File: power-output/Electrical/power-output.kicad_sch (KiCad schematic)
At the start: 27 parts, among them J1 Conn_01x02_Socket, P1 USB_C_Plug_USB2.0, U1 AP2112K-3.3, U2 FUSB302BMPX, U3 LM78L05_SO8, U4 ESP8266EX, U5 CP2102N-Axx-xQFN28

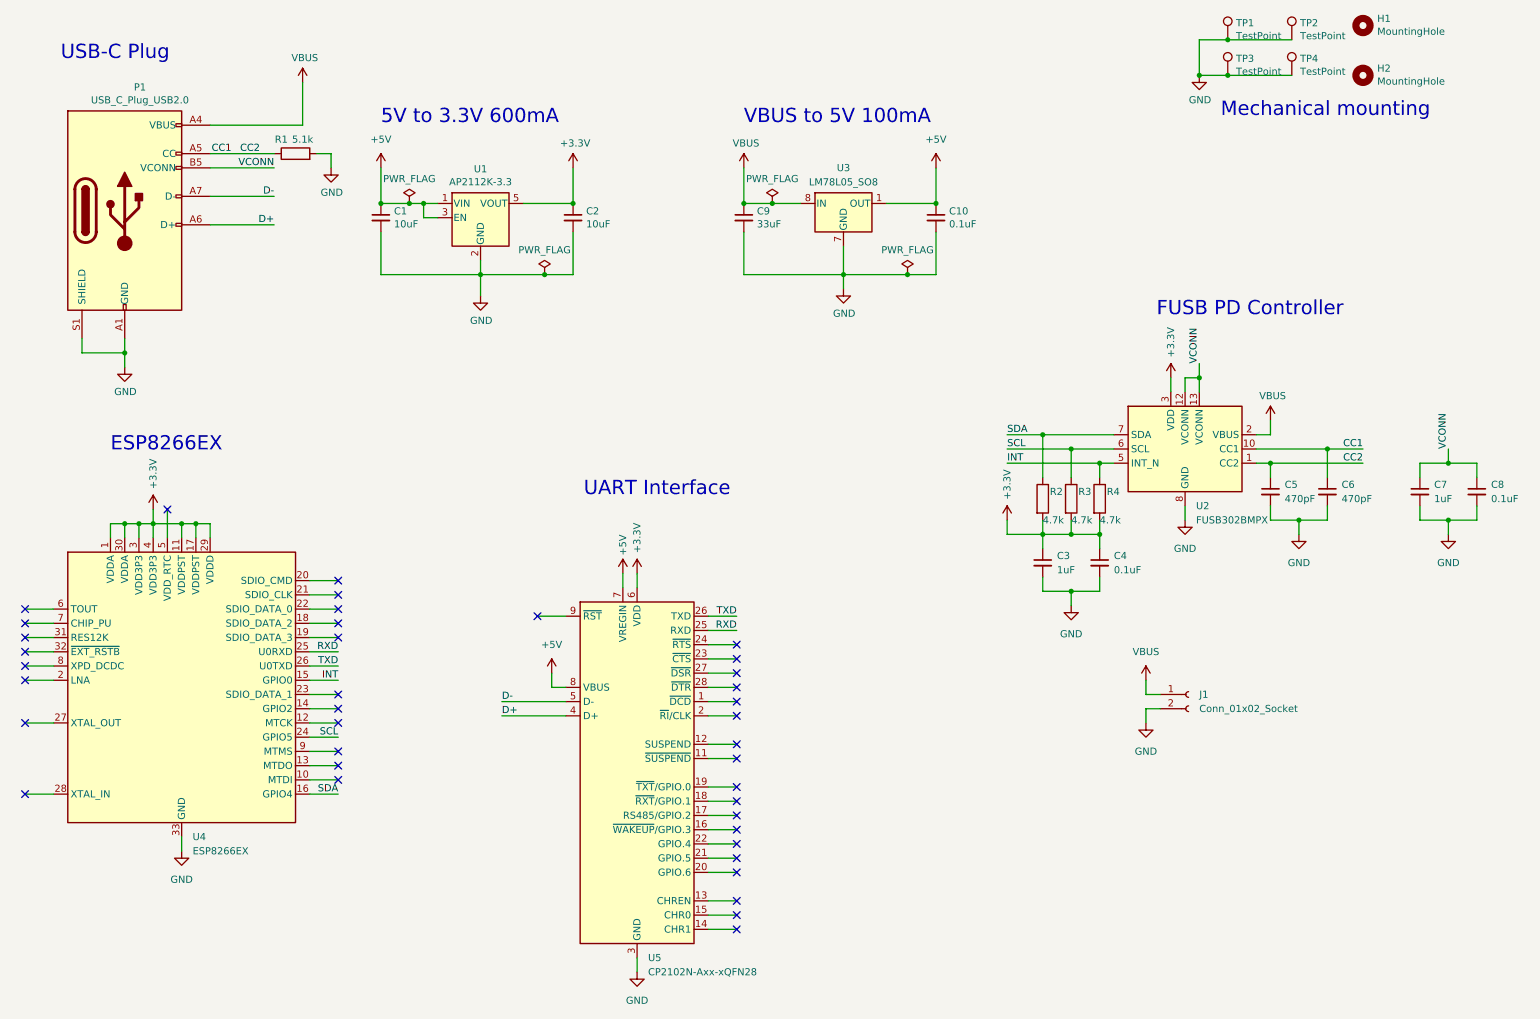
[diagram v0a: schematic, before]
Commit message: Cleaned Up power-output
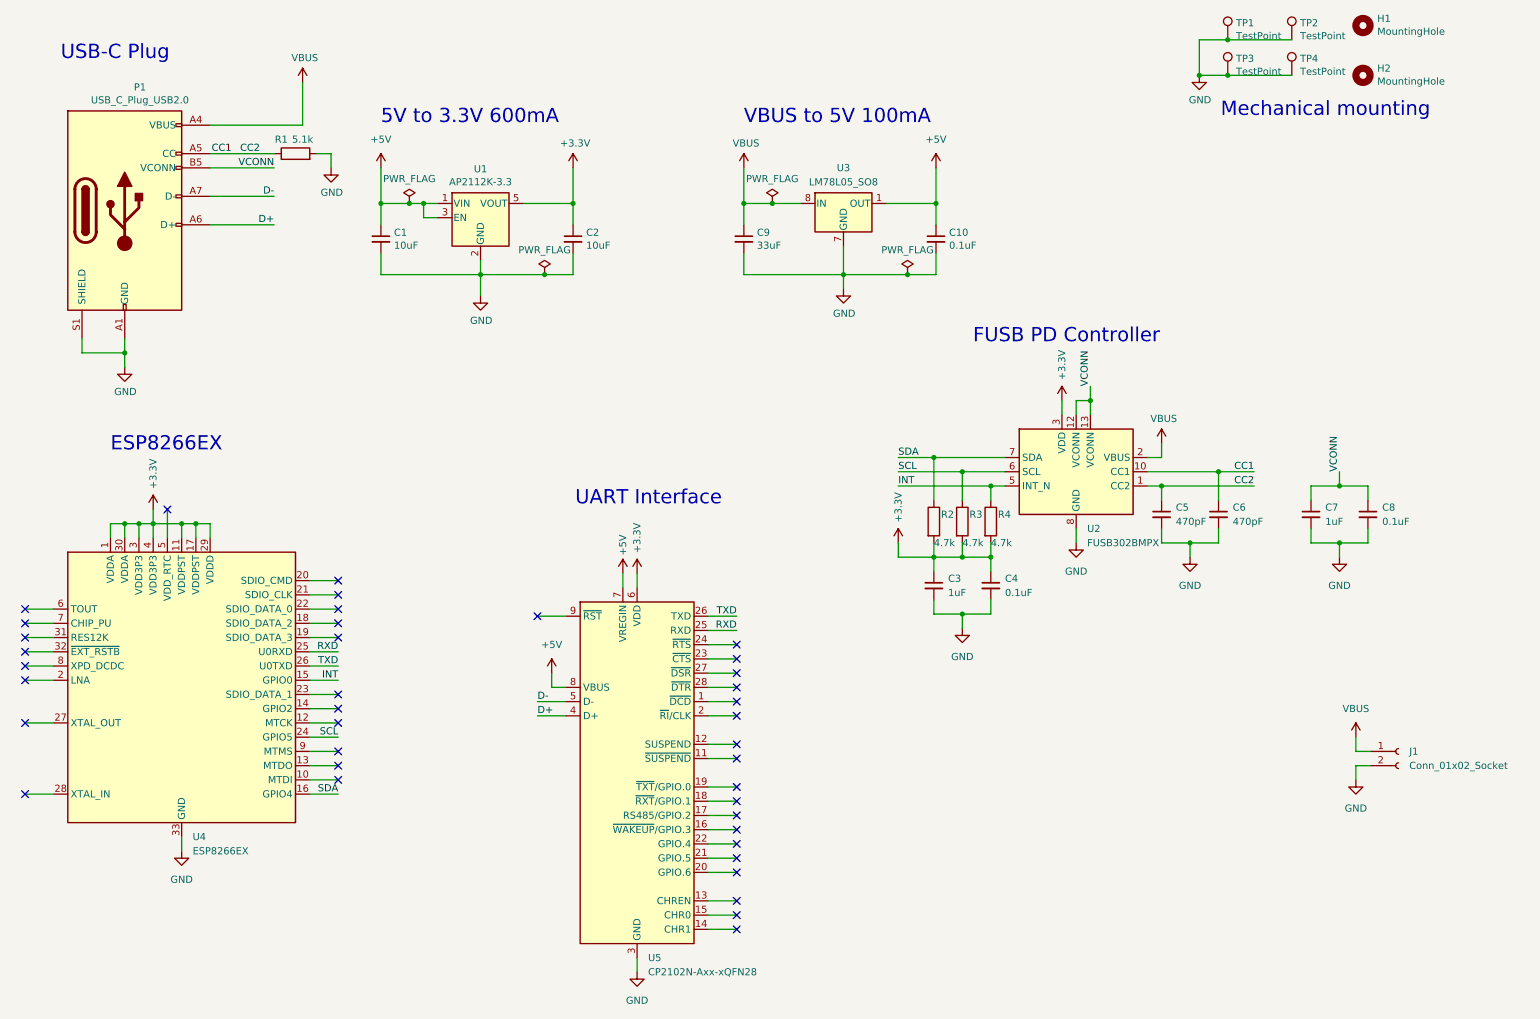
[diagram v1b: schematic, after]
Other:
- moved on the sheet: C1, C10, C2, C3, C4, C5, C6, C7, C8, C9, J1, R2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

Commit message: Cleared Up power-output project
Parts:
- J1: footprint (none) -> Connector_PinSocket_2.54mm:PinSocket_1x02_P2.54mm_Horizontal
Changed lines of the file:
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@@
       (effects (font (size 1.27 1.27)) (justify left))
     )
-    (property "Footprint" "" (at 269.24 149.86 0)
+    (property "Footprint" "Connector_PinSocket_2.54mm:PinSocket_1x02_P2.54mm_Horizontal" (at 269.24 149.86 0)
       (effects (font (size 1.27 1.27)) hide)
     )

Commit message: Cleared power-output project
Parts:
- C1, C2: value 10uF -> 1uF
- C9: value 33uF -> 0.33uF
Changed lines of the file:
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@@
       (effects (font (size 1.27 1.27)) (justify left))
     )
-    (property "Value" "10uF" (at 89.9668 59.563 0)
+    (property "Value" "1uF" (at 89.9668 59.563 0)
       (effects (font (size 1.27 1.27)) (justify left))
     )
@@
       (effects (font (size 1.27 1.27)) (justify left))
     )
-    (property "Value" "10uF" (at 124.2568 59.563 0)
+    (property "Value" "1uF" (at 124.2568 59.563 0)
       (effects (font (size 1.27 1.27)) (justify left))
     )
@@
       (effects (font (size 1.27 1.27)) (justify left))
     )
-    (property "Value" "33uF" (at 154.7368 59.563 0)
-      (effects (font (size 1.27 1.27)) (justify left))
-    )
+    (property "Value" "0.33uF" (at 154.7368 59.563 0)
+      (effects (font (size 1.27 1.27)) (justify left))
+    )

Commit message: Added potential divider
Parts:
- added R5: 9.5k, symbol Device:R
- added R6: 500R, symbol Device:R
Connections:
- net GND: now also R6.2
- net VBUS: now also R5.1
- net at U4.6 (TOUT): now also R5.2, R6.1
- no-connect marks 39 -> 38
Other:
- moved on the sheet: U4
